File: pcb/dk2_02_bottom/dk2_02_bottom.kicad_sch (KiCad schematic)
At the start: 8 parts, among them J1 Conn_01x16_Pin, J2 Conn_01x16_Pin, U1 Pico

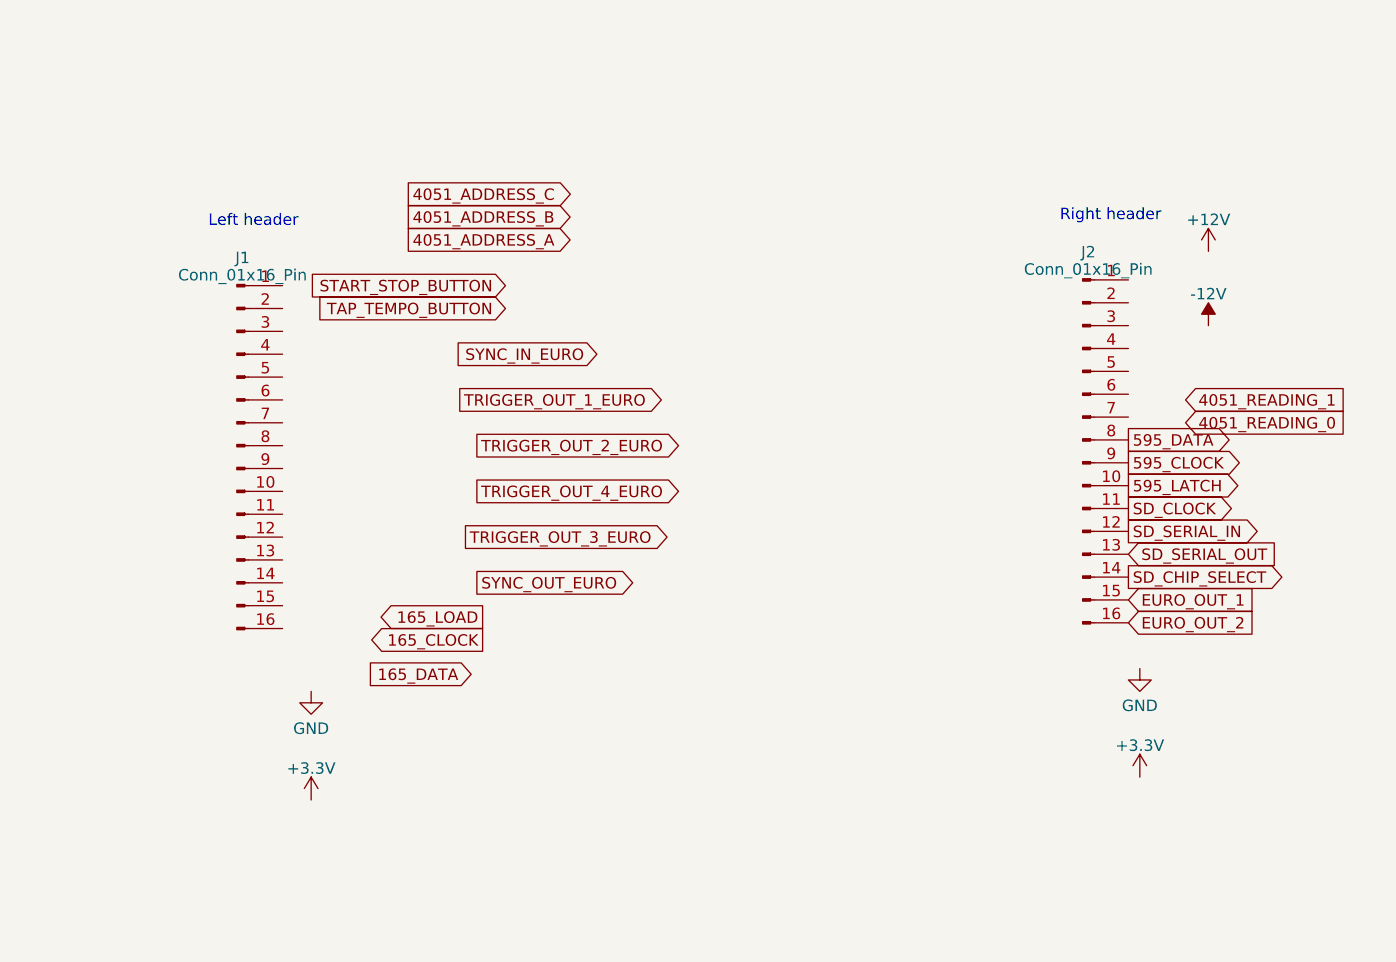
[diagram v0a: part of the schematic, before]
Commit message: bottom pcb looks fairly easy
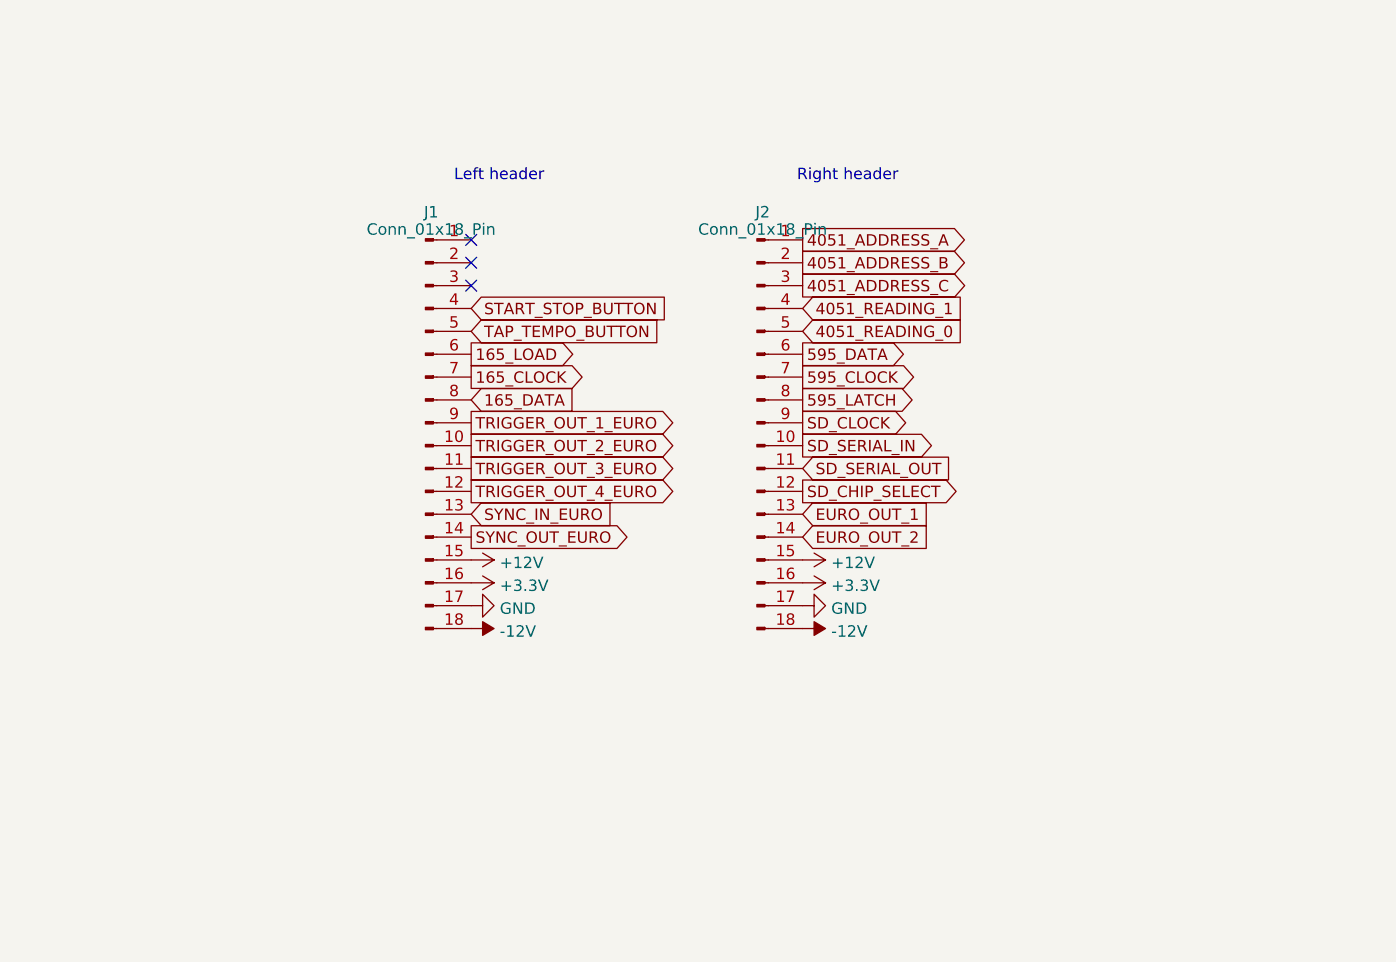
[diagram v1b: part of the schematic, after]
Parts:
- removed J1, J2: Conn_01x16_Pin, symbol Connector:Conn_01x16_Pin
- added J1, J2: Conn_01x18_Pin, Connector_PinHeader_2.54mm:PinHeader_1x18_P2.54mm_Vertical, symbol Connector:Conn_01x18_Pin
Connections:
- net +12V: now also J1.15 (Pin_15), J2.15 (Pin_15)
- net +3.3V: now also J1.16 (Pin_16), J2.16 (Pin_16)
- net -12V: now also J1.18 (Pin_18), J2.18 (Pin_18)
- net 165_CLOCK: now also J1.7 (Pin_7)
- net 165_DATA: now also J1.8 (Pin_8)
- net 165_LOAD: now also J1.6 (Pin_6)
- net 4051_ADDRESS_A: now also J2.1 (Pin_1)
- net 4051_ADDRESS_B: now also J2.2 (Pin_2)
- net 4051_ADDRESS_C: now also J2.3 (Pin_3)
- net 4051_READING_0: now also J2.5 (Pin_5)
- net 4051_READING_1: now also J2.4 (Pin_4)
- net 595_CLOCK: now also J2.7 (Pin_7)
- net 595_DATA: now also J2.6 (Pin_6)
- net 595_LATCH: now also J2.8 (Pin_8)
- net EURO_OUT_1: now also J2.13 (Pin_13)
- net EURO_OUT_2: now also J2.14 (Pin_14)
- net GND: now also J1.17 (Pin_17), J2.17 (Pin_17)
- net SD_CHIP_SELECT: now also J2.12 (Pin_12)
- net SD_CLOCK: now also J2.9 (Pin_9)
- net SD_SERIAL_IN: now also J2.10 (Pin_10)
- net SD_SERIAL_OUT: now also J2.11 (Pin_11)
- net START_STOP_BUTTON: now also J1.4 (Pin_4)
- net SYNC_IN_EURO: now also J1.13 (Pin_13)
- net SYNC_OUT_EURO: now also J1.14 (Pin_14)
- net TAP_TEMPO_BUTTON: now also J1.5 (Pin_5)
- net TRIGGER_OUT_1_EURO: now also J1.9 (Pin_9)
- net TRIGGER_OUT_2_EURO: now also J1.10 (Pin_10)
- net TRIGGER_OUT_3_EURO: now also J1.11 (Pin_11)
- net TRIGGER_OUT_4_EURO: now also J1.12 (Pin_12)
- no-connect marks 6 -> 9

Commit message: done for the week, started routing
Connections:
- net 595_CLOCK: now also J2.11 (Pin_11); no longer J2.7 (Pin_7)
- net 595_DATA: now also J2.10 (Pin_10); no longer J2.6 (Pin_6)
- net 595_LATCH: now also J2.12 (Pin_12); no longer J2.8 (Pin_8)
- net SD_CHIP_SELECT: now also J2.9 (Pin_9); no longer J2.12 (Pin_12)
- net SD_CLOCK: now also J2.6 (Pin_6); no longer J2.9 (Pin_9)
- net SD_SERIAL_IN: now also J2.7 (Pin_7); no longer J2.10 (Pin_10)
- net SD_SERIAL_OUT: now also J2.8 (Pin_8); no longer J2.11 (Pin_11)
